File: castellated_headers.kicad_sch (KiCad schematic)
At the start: 4 parts, among them J2 Conn_01x20, J3 Conn_01x20, J4 Conn_01x20, J6 Conn_01x20

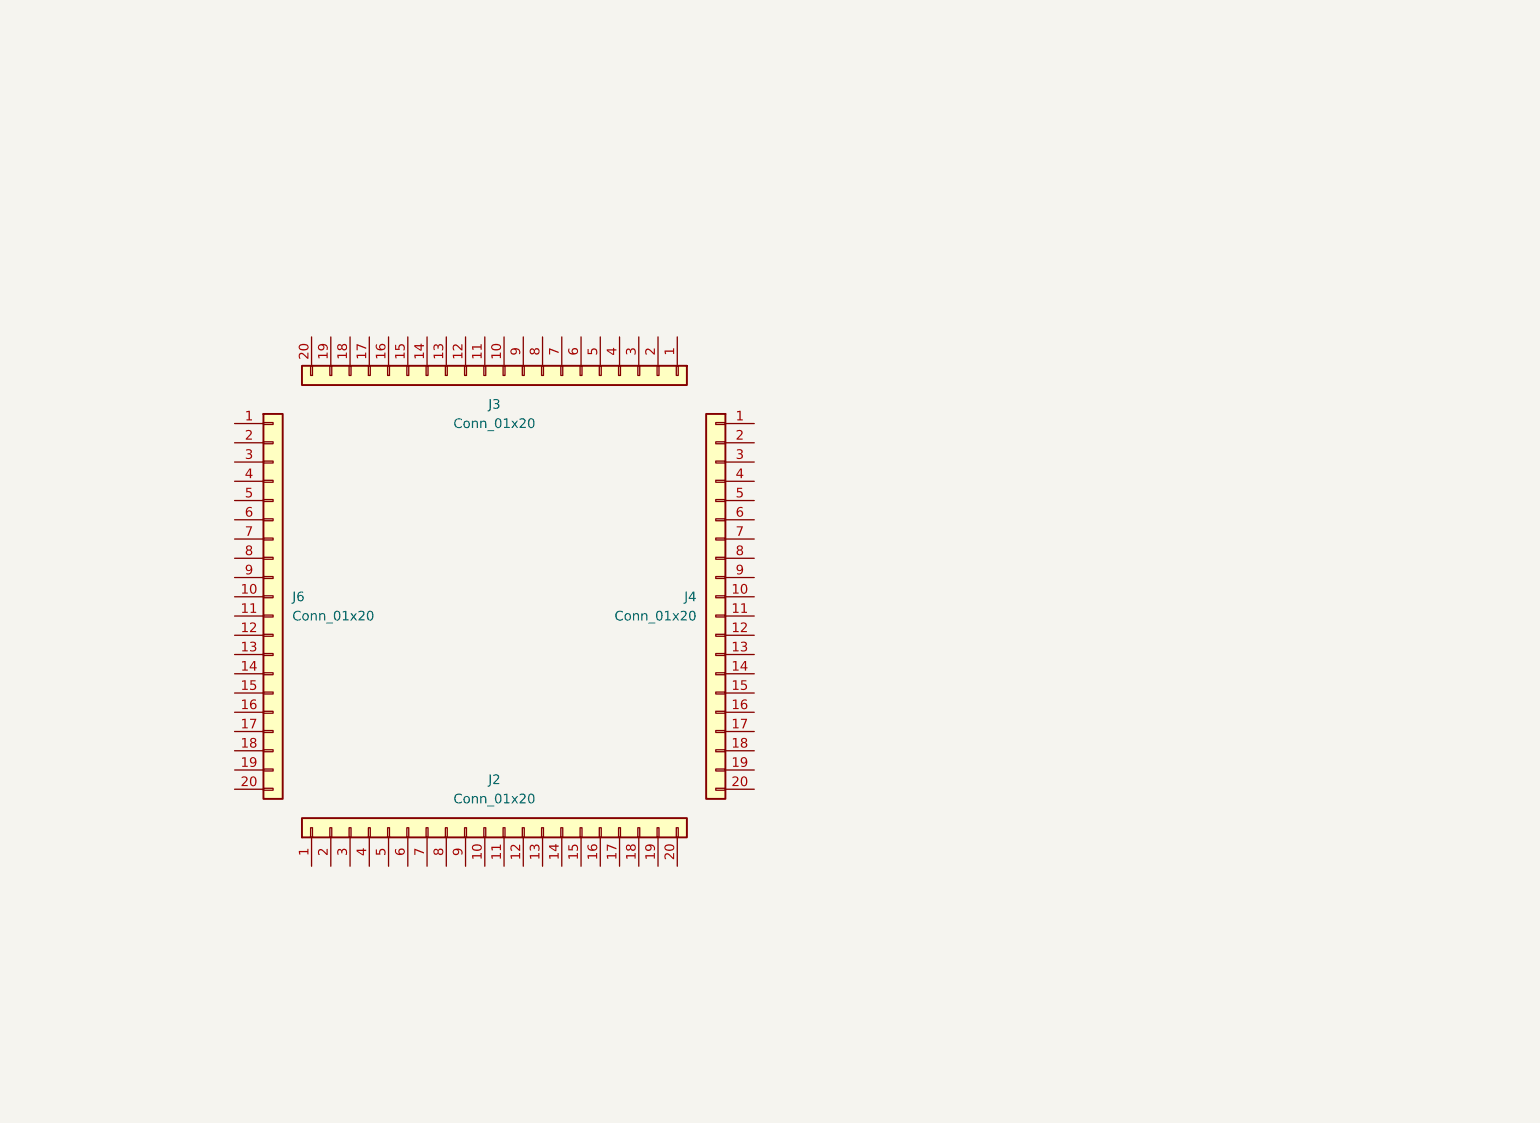
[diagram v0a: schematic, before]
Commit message: Finished LTDC tracks
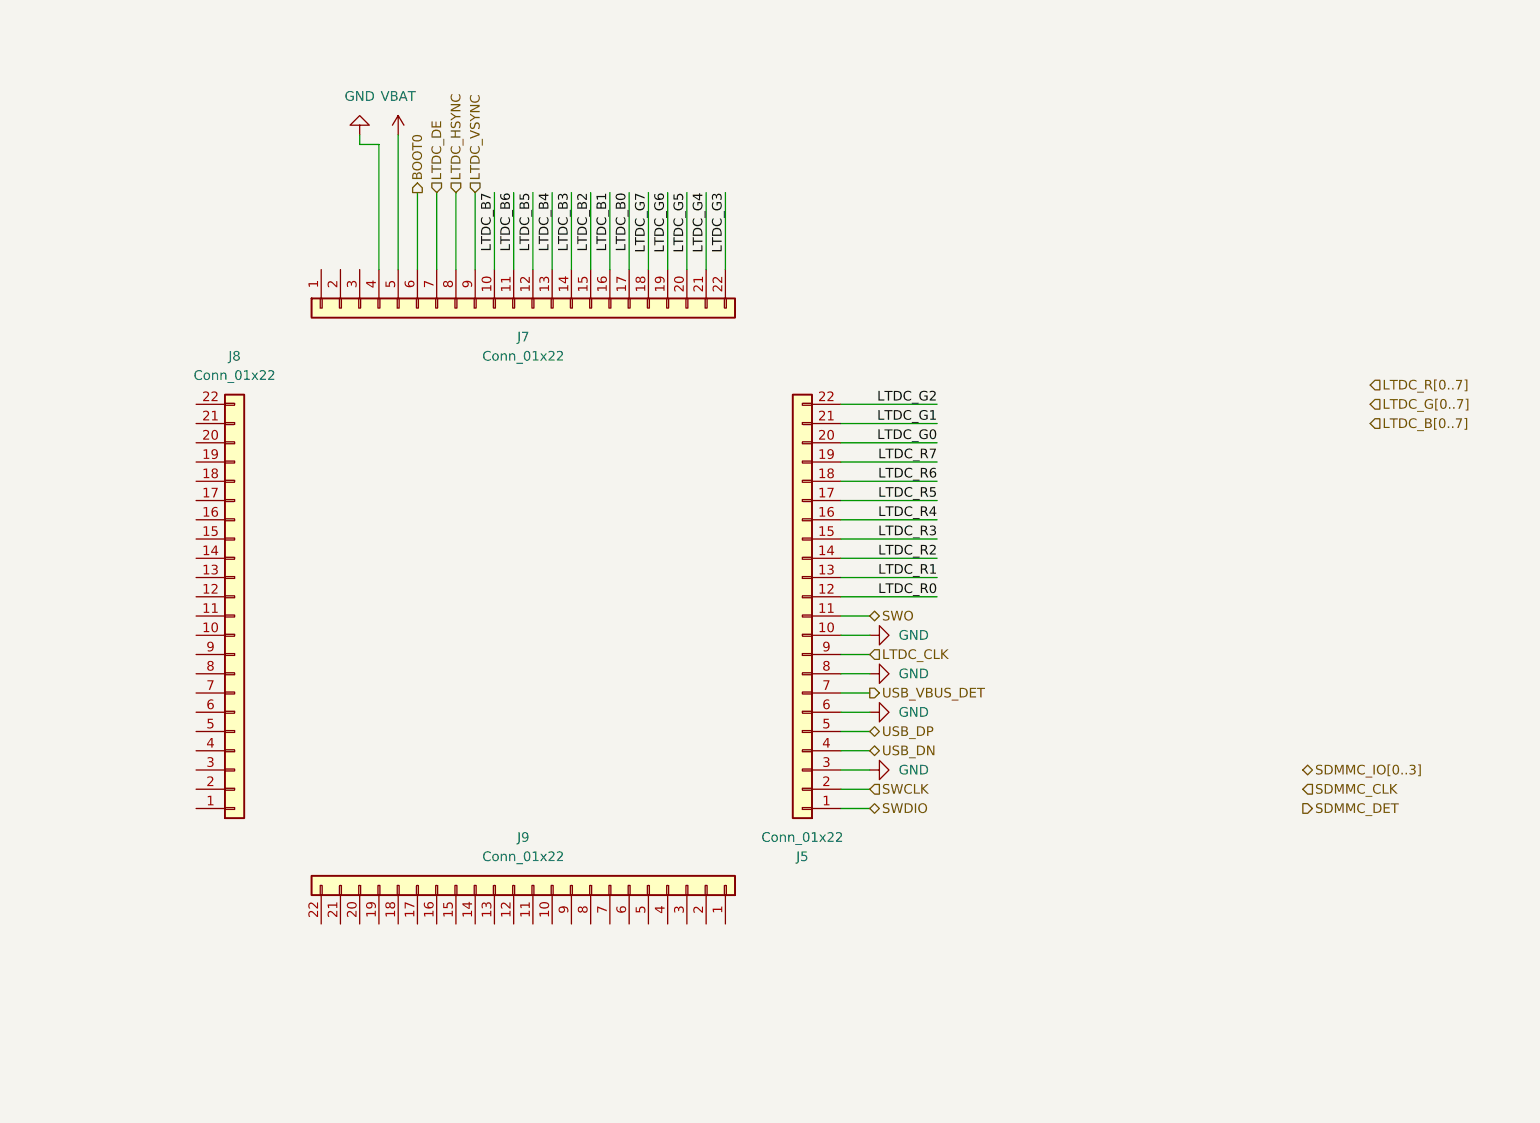
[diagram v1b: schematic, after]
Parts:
- removed J2, J3, J4, J6: Conn_01x20, castellated_holes_header:castellated_01x20_P1.27mm, symbol Connector_Generic:Conn_01x20
- added J5, J7, J8, J9: Conn_01x22, castellated_holes_header:castellated_01x22_P1.27mm, symbol Connector_Generic:Conn_01x22
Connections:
- new net BOOT0: J7.6 (Pin_6)
- new net GND: J5.10 (Pin_10), J5.3 (Pin_3), J5.6 (Pin_6), J5.8 (Pin_8), J7.4 (Pin_4)
- new net LTDC_B0: J7.17 (Pin_17)
- new net LTDC_B1: J7.16 (Pin_16)
- new net LTDC_B2: J7.15 (Pin_15)
- new net LTDC_B3: J7.14 (Pin_14)
- new net LTDC_B4: J7.13 (Pin_13)
- new net LTDC_B5: J7.12 (Pin_12)
- new net LTDC_B6: J7.11 (Pin_11)
- new net LTDC_B7: J7.10 (Pin_10)
- new net LTDC_CLK: J5.9 (Pin_9)
- new net LTDC_DE: J7.7 (Pin_7)
- new net LTDC_G0: J5.20 (Pin_20)
- new net LTDC_G1: J5.21 (Pin_21)
- new net LTDC_G2: J5.22 (Pin_22)
- new net LTDC_G3: J7.22 (Pin_22)
- new net LTDC_G4: J7.21 (Pin_21)
- new net LTDC_G5: J7.20 (Pin_20)
- new net LTDC_G6: J7.19 (Pin_19)
- new net LTDC_G7: J7.18 (Pin_18)
- new net LTDC_HSYNC: J7.8 (Pin_8)
- new net LTDC_R0: J5.12 (Pin_12)
- new net LTDC_R1: J5.13 (Pin_13)
- new net LTDC_R2: J5.14 (Pin_14)
- new net LTDC_R3: J5.15 (Pin_15)
- new net LTDC_R4: J5.16 (Pin_16)
- new net LTDC_R5: J5.17 (Pin_17)
- new net LTDC_R6: J5.18 (Pin_18)
- new net LTDC_R7: J5.19 (Pin_19)
- new net LTDC_VSYNC: J7.9 (Pin_9)
- new net SWCLK: J5.2 (Pin_2)
- new net SWDIO: J5.1 (Pin_1)
- new net SWO: J5.11 (Pin_11)
- new net USB_DN: J5.4 (Pin_4)
- new net USB_DP: J5.5 (Pin_5)
- new net USB_VBUS_DET: J5.7 (Pin_7)
- new net VBAT: J7.5 (Pin_5)

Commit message: test remote connection
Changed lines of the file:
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@@
+		)
+	)
+	(hierarchical_label "SDMMC_CMD"
+		(shape input)
+		(at 217.17 125.73 0)
+		(fields_autoplaced yes)
+		(effects
+			(font
+				(size 1.27 1.27)
+			)
+			(justify left)
 		)
 	)

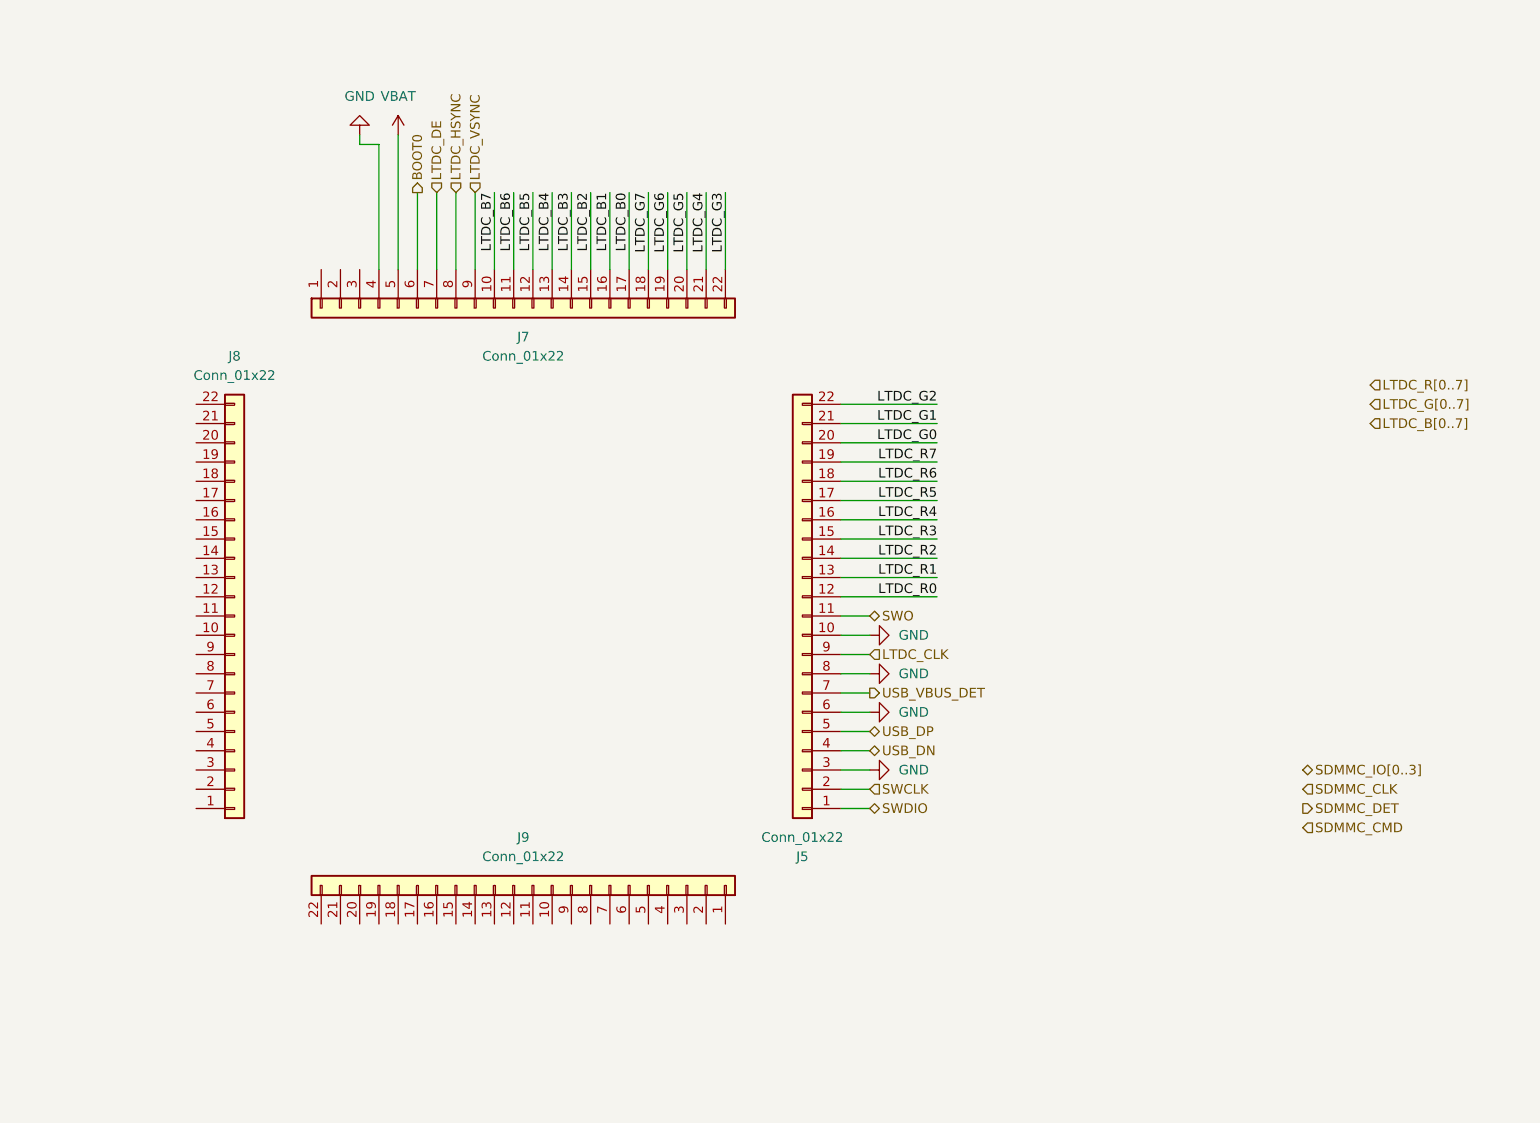
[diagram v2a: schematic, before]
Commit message: Finished fanout all remaining pin, Power block left
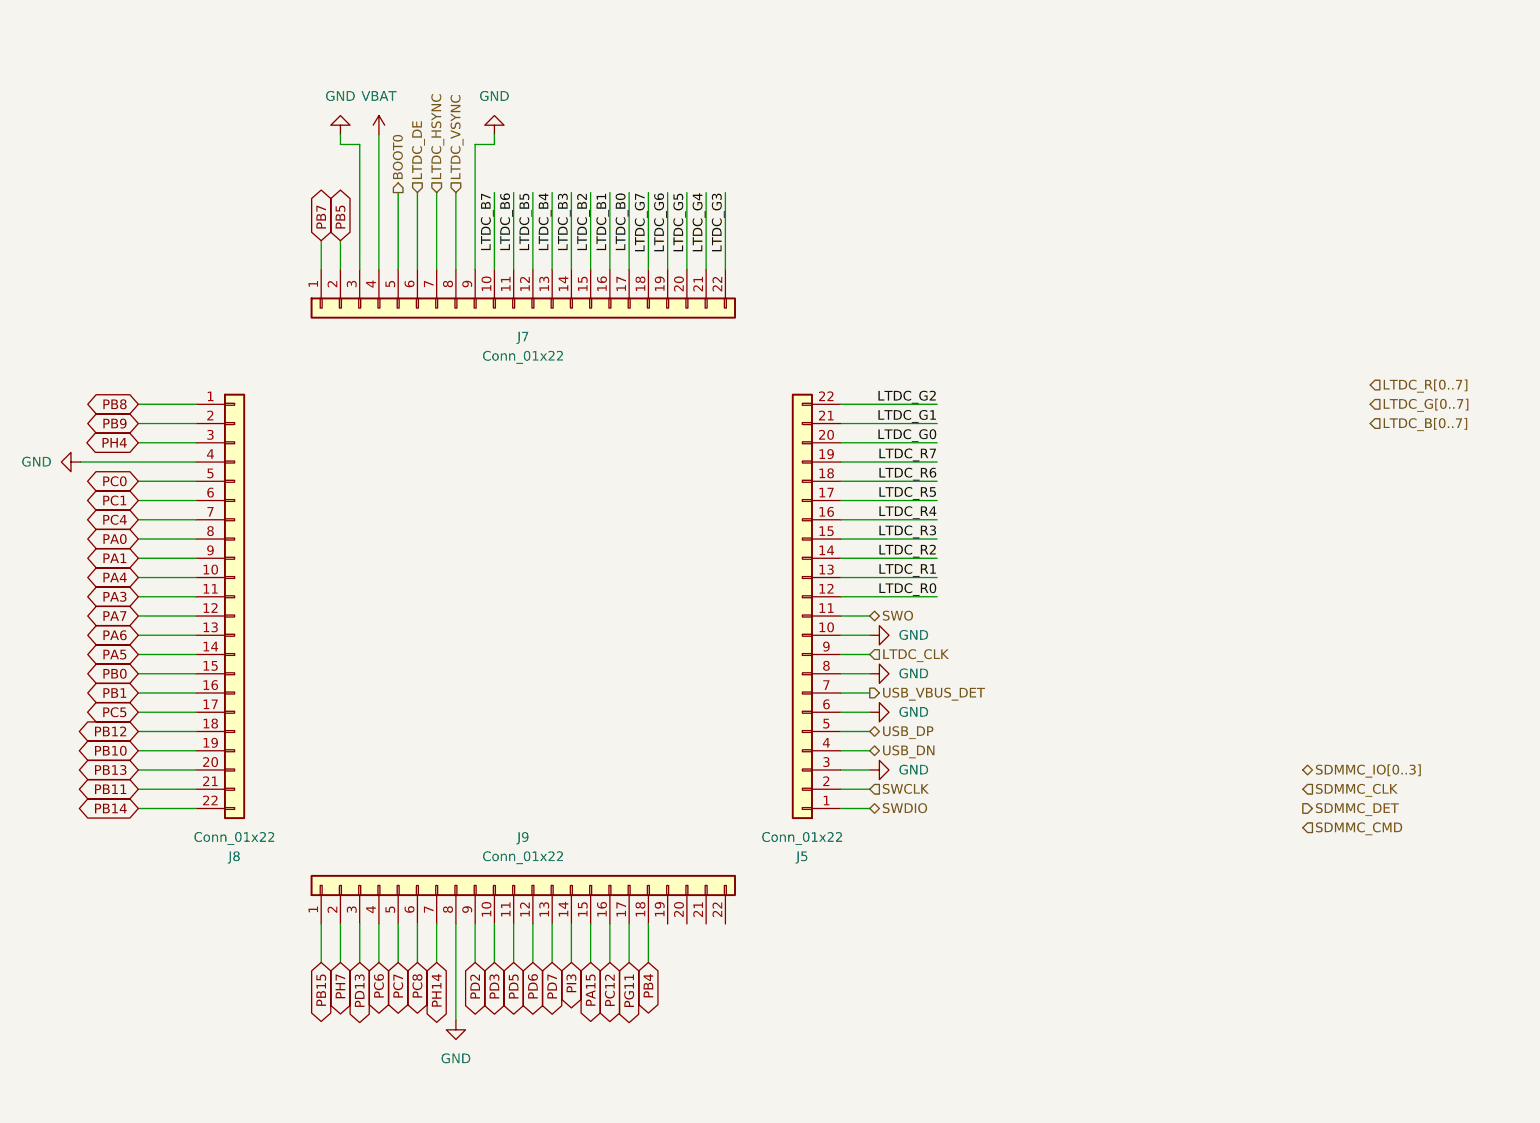
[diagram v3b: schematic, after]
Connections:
- net BOOT0: now also J7.5 (Pin_5); no longer J7.6 (Pin_6)
- net GND: now also J7.3 (Pin_3), J7.9 (Pin_9), J8.4 (Pin_4), J9.8 (Pin_8); no longer J7.4 (Pin_4)
- net LTDC_DE: now also J7.6 (Pin_6); no longer J7.7 (Pin_7)
- net LTDC_HSYNC: now also J7.7 (Pin_7); no longer J7.8 (Pin_8)
- net LTDC_VSYNC: now also J7.8 (Pin_8); no longer J7.9 (Pin_9)
- net VBAT: now also J7.4 (Pin_4); no longer J7.5 (Pin_5)
- net PB8: now reaches J8.1 (Pin_1)
- net PA4: now reaches J8.10 (Pin_10)
- net PA3: now reaches J8.11 (Pin_11)
- net PA7: now reaches J8.12 (Pin_12)
- net PA6: now reaches J8.13 (Pin_13)
- net PA5: now reaches J8.14 (Pin_14)
- net PB0: now reaches J8.15 (Pin_15)
- net PB1: now reaches J8.16 (Pin_16)
- net PC5: now reaches J8.17 (Pin_17)
- net PB12: now reaches J8.18 (Pin_18)
- net PB10: now reaches J8.19 (Pin_19)
- net PB9: now reaches J8.2 (Pin_2)
- net PB13: now reaches J8.20 (Pin_20)
- net PB11: now reaches J8.21 (Pin_21)
- net PB14: now reaches J8.22 (Pin_22)
- net PH4: now reaches J8.3 (Pin_3)
- net PC0: now reaches J8.5 (Pin_5)
- net PC1: now reaches J8.6 (Pin_6)
- net PC4: now reaches J8.7 (Pin_7)
- net PA0: now reaches J8.8 (Pin_8)
- net PA1: now reaches J8.9 (Pin_9)
- net PB15: now reaches J9.1 (Pin_1)
- net PD3: now reaches J9.10 (Pin_10)
- net PD5: now reaches J9.11 (Pin_11)
- net PD6: now reaches J9.12 (Pin_12)
- net PD7: now reaches J9.13 (Pin_13)
- net PI3: now reaches J9.14 (Pin_14)
- net PA15: now reaches J9.15 (Pin_15)
- net PC12: now reaches J9.16 (Pin_16)
- net PG11: now reaches J9.17 (Pin_17)
- net PB4: now reaches J9.18 (Pin_18)
- net PH7: now reaches J9.2 (Pin_2)
- net PD13: now reaches J9.3 (Pin_3)
- net PC6: now reaches J9.4 (Pin_4)
- net PC7: now reaches J9.5 (Pin_5)
- net PC8: now reaches J9.6 (Pin_6)
- net PH14: now reaches J9.7 (Pin_7)
- net PD2: now reaches J9.9 (Pin_9)
- net PB7: now reaches J7.1 (Pin_1)
- net PB5: now reaches J7.2 (Pin_2)
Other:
- moved on the sheet: J9

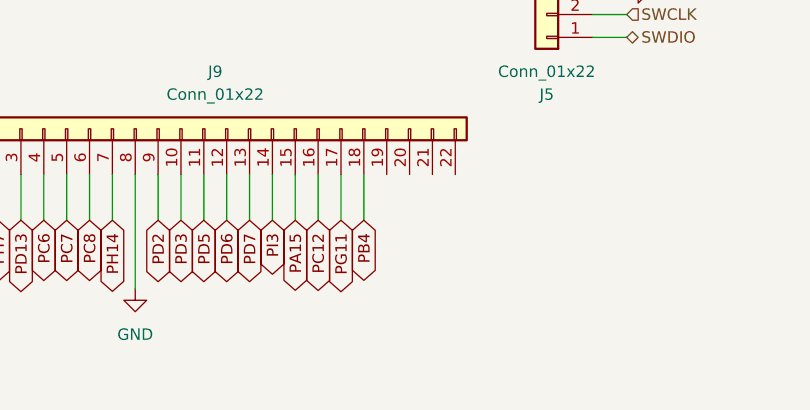
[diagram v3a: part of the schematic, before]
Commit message: Changed PMIC to dc-dc converter, finished track
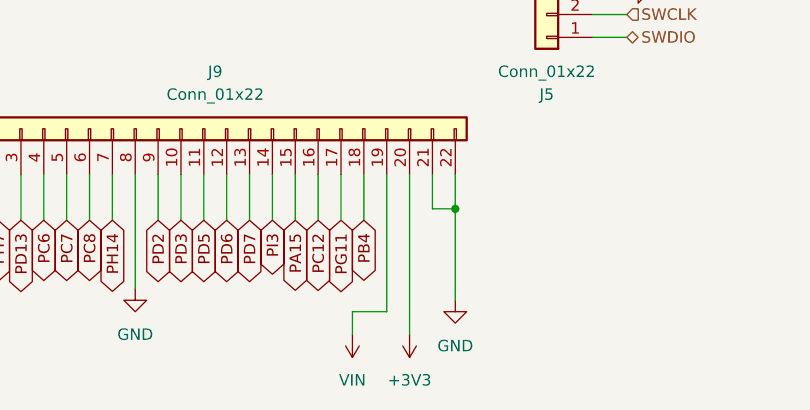
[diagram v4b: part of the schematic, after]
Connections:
- net GND: now also J9.21 (Pin_21), J9.22 (Pin_22)
- net VIN: now reaches J9.19 (Pin_19)
- net +3V3: now reaches J9.20 (Pin_20)

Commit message: generate doc
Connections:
- net GND: now also J7.2 (Pin_2), J8.5 (Pin_5); no longer J7.3 (Pin_3), J8.4 (Pin_4), J9.8 (Pin_8)
- net PA0: now also J8.9 (Pin_9); no longer J8.8 (Pin_8)
- net PA1: now also J8.10 (Pin_10); no longer J8.9 (Pin_9)
- net PA3: now also J8.12 (Pin_12); no longer J8.11 (Pin_11)
- net PA4: now also J8.11 (Pin_11); no longer J8.10 (Pin_10)
- net PA5: now also J8.15 (Pin_15); no longer J8.14 (Pin_14)
- net PA6: now also J8.14 (Pin_14); no longer J8.13 (Pin_13)
- net PA7: now also J8.13 (Pin_13); no longer J8.12 (Pin_12)
- net PB0: now also J8.16 (Pin_16); no longer J8.15 (Pin_15)
- net PB1: now also J8.17 (Pin_17); no longer J8.16 (Pin_16)
- net PB10: now also J8.20 (Pin_20); no longer J8.19 (Pin_19)
- net PB11: now also J8.22 (Pin_22); no longer J8.21 (Pin_21)
- net PB12: now also J8.19 (Pin_19); no longer J8.18 (Pin_18)
- net PB13: now also J8.21 (Pin_21); no longer J8.20 (Pin_20)
- net PB14: now also J9.1 (Pin_1); no longer J8.22 (Pin_22)
- net PB15: now also J9.2 (Pin_2); no longer J9.1 (Pin_1)
- net PB5: now also J7.1 (Pin_1); no longer J7.2 (Pin_2)
- net PB7: now also J8.1 (Pin_1); no longer J7.1 (Pin_1)
- net PB8: now also J8.2 (Pin_2); no longer J8.1 (Pin_1)
- net PB9: now also J8.3 (Pin_3); no longer J8.2 (Pin_2)
- net PC0: now also J8.6 (Pin_6); no longer J8.5 (Pin_5)
- net PC1: now also J8.7 (Pin_7); no longer J8.6 (Pin_6)
- net PC4: now also J8.8 (Pin_8); no longer J8.7 (Pin_7)
- net PC5: now also J8.18 (Pin_18); no longer J8.17 (Pin_17)
- net PC6: now also J9.5 (Pin_5); no longer J9.4 (Pin_4)
- net PC7: now also J9.6 (Pin_6); no longer J9.5 (Pin_5)
- net PC8: now also J9.7 (Pin_7); no longer J9.6 (Pin_6)
- net PD13: now also J9.4 (Pin_4); no longer J9.3 (Pin_3)
- net PH14: now also J9.8 (Pin_8); no longer J9.7 (Pin_7)
- net PH4: now also J8.4 (Pin_4); no longer J8.3 (Pin_3)
- net PH7: now also J9.3 (Pin_3); no longer J9.2 (Pin_2)
- net VBAT renamed NRST
- new net VRTC: J7.3 (Pin_3)

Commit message: 98% finished, st-link part left
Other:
- note added: "PA11"
- note added: "PA12"
- note added: "PA2"
- note added: "PA8"
- note added: "PA9"
- note added: "PC10"
- note added: "PC9"
- note added: "PE4"
- note added: "PE5"
- note added: "PE6"
- note added: "PF10"
- note added: "PG10"
- note added: "PG12"
- note added: "PG13"
- note added: "PG6"
- note added: "PG7"
- note added: "PH10"
- note added: "PH11"
- note added: "PH12"
- note added: "PH13"
- note added: "PH15"
- note added: "PH9"
- note added: "PI0"
- note added: "PI1"
- note added: "PI10"
- note added: "PI2"
- note added: "PI4"
- note added: "PI5"
- note added: "PI6"
- note added: "PI7"
- note added: "PI9"
